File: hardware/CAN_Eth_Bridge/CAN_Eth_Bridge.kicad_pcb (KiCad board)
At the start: 2 copper layers, 60 x 100 mm, 161 parts, among them J101 Main Current Hall Sensor, J102 Global LV and CAN, J103 HRLV, J105 Conn_02x05_Odd_Even, J106 uart, J107 Micro_SD_Card, J301 RJ45_Amphenol_RJMG1BD3B8K1ANR, K101 G5Q-1A 24Vdc, Q101 MMBT5550L, Q102 MMBT5550L, Q103 MMBT5550L, Q301 MMBT5550L, Q302 MMBT5550L, Q501 MMBT5550L, Q502 MMBT5550L, U101 MCP2542FDxMF, U102 MCP2542FDxMF, U105 XM0G3507QPTRQ1, U201 Si1450DH, U202 LM74502, U203 Si1450DH, U204 AP64060ZQ, U205 AP64060ZQ, U301 W5500, U401 MCP1501-40xSN, U402 TLV713185PDBV, U404 MCP33151, U405 MCP33151, U408 Si1450DH, U409 NCV68061, U501 NSI5030, U502 Si1450DH, U503 NCV68061, U504 MCP2542FDxMF, U505 AP7384-50SA, U506 ISOM8110, U507 ISOM8110, U508 STISO620, Y301 Crystal_GND24

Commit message: long 88 can stick
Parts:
- removed C201, C208, C321, C401, C402, C403, C404, C408, C409, C410, C501, C504, C505, C506: 220n, Capacitor_SMD:C_0805_2012Metric_Pad1.18x1.45mm_HandSolder
- removed C203, C205, C206, C207, C209, C211, C212, C213: 10u, Capacitor_SMD:C_1206_3216Metric_Pad1.33x1.80mm_HandSolder
- removed C204, C210: 100n, Capacitor_SMD:C_1206_3216Metric_Pad1.33x1.80mm_HandSolder
- removed C406: 10n, Capacitor_SMD:C_0805_2012Metric_Pad1.18x1.45mm_HandSolder
- removed C502, C503: 1u, Capacitor_SMD:C_1206_3216Metric_Pad1.33x1.80mm_HandSolder
- removed D102, D201, D202: green, LED_SMD:LED_0805_2012Metric_Pad1.15x1.40mm_HandSolder
- removed D203, D204: ES1D, Diode_SMD:D_SMA
- removed D501, D502, D503: TS4148, Diode_SMD:D_0805_2012Metric_Pad1.15x1.40mm_HandSolder
- removed D504: 10V, Diode_SMD:D_0805_2012Metric_Pad1.15x1.40mm_HandSolder
- removed F101: ~1A, Fuse:Fuseholder_Blade_Mini_Keystone_3568
- removed J103: HRLV, Connector_Molex:Molex_Micro-Fit_3.0_43045-0600_2x03_P3.00mm_Horizontal
- removed J105: Conn_02x05_Odd_Even, Connector_PinHeader_1.27mm:PinHeader_2x05_P1.27mm_Vertical_SMD
- removed J106: uart, Connector_PinHeader_2.54mm:PinHeader_1x03_P2.54mm_Vertical
- removed J107: Micro_SD_Card, Connector_Card:microSD_HC_Wuerth_693072010801
- removed K101: G5Q-1A 24Vdc, Relay_THT:Relay_SPST_Omron-G5Q-1A
- removed L201, L202: 10u, Inductor_SMD:L_1210_3225Metric_Pad1.42x2.65mm_HandSolder
- removed Q101, Q102, Q103, Q501, Q502: MMBT5550L, Package_TO_SOT_SMD:SOT-23
- removed R1, R2, R505: 100, Resistor_SMD:R_1206_3216Metric_Pad1.30x1.75mm_HandSolder
- removed R102, R201: 4.99k, Resistor_SMD:R_1206_3216Metric_Pad1.30x1.75mm_HandSolder
- removed R104, R202, R501: 88.7k, Resistor_SMD:R_0805_2012Metric_Pad1.20x1.40mm_HandSolder
- removed R105, R203, R204: 3.32k, Resistor_SMD:R_0805_2012Metric_Pad1.20x1.40mm_HandSolder
- removed R106: 49.9, Resistor_SMD:R_0805_2012Metric_Pad1.20x1.40mm_HandSolder
- removed R205: 140k, Resistor_SMD:R_0805_2012Metric_Pad1.20x1.40mm_HandSolder
- removed R206, R208, R211: 22.1k, Resistor_SMD:R_0805_2012Metric_Pad1.20x1.40mm_HandSolder
- removed R207: 88.7kR, Resistor_SMD:R_0805_2012Metric_Pad1.20x1.40mm_HandSolder
- removed R209, R212: 4.7, Resistor_SMD:R_1206_3216Metric_Pad1.30x1.75mm_HandSolder
- removed R210: 51k, Resistor_SMD:R_0805_2012Metric_Pad1.20x1.40mm_HandSolder
- removed R404, R405: 14.3, Resistor_SMD:R_0805_2012Metric_Pad1.20x1.40mm_HandSolder
- removed R502, R503, R506: 2.4k, Resistor_SMD:R_0805_2012Metric_Pad1.20x1.40mm_HandSolder
- removed U105: XM0G3507QPTRQ1, zzLocalLibraries-Footprints:PT0048A-IPC_B
- removed U201, U203, U408: Si1450DH, Package_TO_SOT_SMD:SOT-363_SC-70-6_Handsoldering
- removed U202: LM74502, Package_TO_SOT_SMD:SOT-23-8_Handsoldering
- removed U204, U205: AP64060ZQ, Package_TO_SOT_SMD:TSOT-23-6
- removed U401: MCP1501-40xSN, Package_SO:SOIC-8_3.9x4.9mm_P1.27mm
- removed U402: TLV713185PDBV, Package_TO_SOT_SMD:SOT-23-5
- removed U404, U405: MCP33151, Package_SO:MSOP-10_3x3mm_P0.5mm
- removed U409, U503: NCV68061, Package_TO_SOT_SMD:TSOT-23-6
- removed U501: NSI5030, Diode_SMD:Nexperia_CFP3_SOD-123W
- removed U502: Si1450DH, Package_TO_SOT_SMD:SOT-363_SC-70-6
- removed U504: MCP2542FDxMF, Package_SO:SOIC-8_3.9x4.9mm_P1.27mm
- removed U505: AP7384-50SA, Package_TO_SOT_SMD:SOT-23
- removed U506, U507: ISOM8110, zzLocalLibraries-Footprints:ISOM811_SOIC-4_DFG
- removed U508: STISO620, Package_SO:SOIC-8_7.5x5.85mm_P1.27mm
- added C103: 220n, Capacitor_SMD:C_0805_2012Metric_Pad1.18x1.45mm_HandSolder, F.Cu at (94.9, 114.6)
- added FL102: Choke_CommonMode_FerriteCore_1243, Inductor_SMD:L_CommonModeChoke_Coilcraft_1812CAN, F.Cu at (112.1, 116.0)
- added SW102: SW_DIP_x06, Button_Switch_SMD:SW_DIP_SPSTx06_Slide_Copal_CHS-06B_W7.62mm_P1.27mm, F.Cu at (97.9, 107.9)
- added U103: XMSM0G3507SDGS28R, zzLocalLibraries-Footprints:VSSOP28_DGS_TEX-M, F.Cu at (107.5, 107.2)
- added U104: AP7381-33SA-7, Package_TO_SOT_SMD:SOT-23, F.Cu at (105.7, 114.3)
- J101: value Main Current Hall Sensor -> Conn_01x05_Pin; footprint Connector_Molex:Molex_Micro-Fit_3.0_43045-0400_2x02_P3.00mm_Horizontal -> Connector_PinHeader_2.54mm:PinHeader_1x05_P2.54mm_Vertical
- U102: value MCP2542FDxMF -> AP7384-50SA; footprint Package_SO:SOIC-8_3.9x4.9mm_P1.27mm -> Package_TO_SOT_SMD:SOT-23-3
- moved H103 108.6 mm to (100.9, 89.4)
- moved C101 100.3 mm to (94.5, 78.9), turned to 0 degrees
- moved C102 98.0 mm to (94.5, 82.0), turned to 0 degrees
- moved U102 91.5 mm to (99.5, 99.0), turned to 0 degrees
- moved C104 84.7 mm to (94.5, 85.0), turned to 0 degrees
- moved H102 81.8 mm to (100.9, 81.4)
- moved C110 80.8 mm to (94.5, 94.0)
- moved C109 80.6 mm to (94.5, 91.0)
- moved C108 79.9 mm to (94.5, 88.0), turned to 0 degrees
- moved U101 76.1 mm to (109.1, 96.0)
- moved J102 75.2 mm to (147.7, 137.9), turned to 180 degrees
- moved R111 73.5 mm to (99.9, 95.0), turned to 0 degrees
- moved R108 70.7 mm to (112.1, 81.9)
- moved D104 70.0 mm to (107.3, 85.0), turned to 0 degrees
- moved R110 68.7 mm to (112.1, 87.8), turned to 0 degrees
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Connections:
- C101 pad 1: +5V -> +3.3V
- C102 pad 1: +3.3V -> +5V
- D101 pad 1: LV+ -> Net-(D101-K)
- D101 pad 2: Net-(D101-A) -> /GLV+
- J101 pad 1: /MCHall_5Vin -> GND
- J101 pad 2: GND -> /prog.uart_ui_rx
- J101 pad 3: /MCHall_imprecise -> /prog.uart_ui_tx
- J101 pad 4: /MCHall_percise -> /prog.SWDIO
- J102 pad 4: /G_IL- -> /G_IL+
- U101 pad 6: /G_CAN- -> Net-(U101-CANL)
- U101 pad 7: /G_CAN+ -> Net-(U101-CANH)
- U102 pad 1: /HRLV interface/CAN_RX -> Net-(D101-K)
- U102 pad 2: GND -> +5V
- U102 pad 3: +5V -> GND
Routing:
- net (no net): track 0.00 -> 186.6 mm, vias 0 -> 2
- net +3.3V: track 304.3 -> 132.7 mm, vias 9 -> 2
- net +5V: track 124.4 -> 0.00 mm
- net LV+: track 80.2 -> 0.00 mm
- net /G_CAN+: track 67.4 -> 0.00 mm, vias 2 -> 0
- net /G_CAN-: track 67.4 -> 0.00 mm, vias 2 -> 0
- net /HRLV interface/+5V: track 66.0 -> 0.00 mm
- net /HRLV interface/LV+: track 54.7 -> 0.00 mm
- net /hrlv.pres_hrlv: track 48.2 -> 0.00 mm, vias 2 -> 0
- net /IL.forward: track 47.6 -> 0.00 mm
- net Net-(D102-K): track 41.4 -> 0.00 mm
- net /GLV PSU/GLV+: track 41.2 -> 0.00 mm
- net /hrlv.pres_interlock: track 37.3 -> 0.00 mm, vias 2 -> 0
- net /prog.uart_ui_rx: track 29.2 -> 4.57 mm, vias 2 -> 0
- net /Main Current Hall Sensing/4.096Vref: track 23.9 -> 0.00 mm
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- removed copper zone on F.Cu, net /GLV PSU/passing
- removed copper zone on B.Cu, net /G_IL+
- removed copper zone on F.Cu, net /G_IL+
- removed copper zone on B.Cu, net /G_IL-
- removed copper zone on F.Cu, net /G_IL-
- removed copper zone on B.Cu, net /HRLV_LV-
- removed copper zone on F.Cu, net /HRLV_LV-
- removed copper zone on F.Cu, net /vcore
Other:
- board size 60 x 100 mm -> 23 x 85 mm
- board text removed: "600Vdc galv ISO"
- board text removed: "CAN+"
- board text removed: "CAN-"
- board text removed: "GLV+ (9,34)V"
- board text removed: "GLV-"
- board text removed: "HRLV interface"
- board text removed: "IL return"
- board text removed: "IL_B"
- board text removed: "LV+ (5.5 , 35)V"
- board text removed: "LV-"
- board text removed: "bms fault"
- board text removed: "fuse ~800mA"
- board text removed: "ground loop from LV bulk to diode crosses sense line"
- board text removed: "indicator 2"

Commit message: shuffled
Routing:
- net (no net): track 186.6 -> 2.53 mm, vias 2 -> 0
- net /eth.MOSI/PICO: track 20.2 -> 1.71 mm, vias 2 -> 0
- net /eth.MISO/POCI: track 18.2 -> 2.49 mm, vias 2 -> 0
- net +3.3V: track 132.7 -> 117.0 mm, vias 2 -> 1
- net /eth.irq_N: track 15.5 -> 0.05 mm
- net /eth.reset_N: track 14.5 -> 0.00 mm
- net /eth.SCLK: track 17.5 -> 3.05 mm
- net /eth.cs_N: track 18.5 -> 5.93 mm
- net GND: track 24.7 -> 16.7 mm, vias 82 -> 61
- net /G_IL+: track 5.27 -> 0.00 mm
- net /prog.uart_ui_tx: track 4.67 -> 0.00 mm
- net /prog.uart_ui_rx: track 4.57 -> 0.00 mm
- net /GLV+: track 2.73 -> 0.00 mm
- removed copper zone on F.Cu, net +3.3V
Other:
- board size 23 x 85 mm -> 22.6 x 85 mm
- board text removed: "indicator 1"
- board text removed: "scheduler"

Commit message: hdd failure D:
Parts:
- removed C102, C108, C109, C110, C315: 220n, Capacitor_SMD:C_0805_2012Metric_Pad1.18x1.45mm_HandSolder
- removed C107: 10u, Capacitor_SMD:C_1206_3216Metric_Pad1.33x1.80mm_HandSolder
- removed C307, C308, C310: 100n, Capacitor_SMD:C_0603_1608Metric_Pad1.08x0.95mm_HandSolder
- removed D103, D104: yellow, LED_SMD:LED_0805_2012Metric_Pad1.15x1.40mm_HandSolder
- removed D106: blue, LED_SMD:LED_0805_2012Metric_Pad1.15x1.40mm_HandSolder
- removed FL102: Choke_CommonMode_FerriteCore_1243, Inductor_SMD:L_CommonModeChoke_Coilcraft_1812CAN
- removed H101, H102, H103: MountingHole, MountingHole:MountingHole_3.2mm_M3
- removed R107, R108, R109: 2.4k, Resistor_SMD:R_0805_2012Metric_Pad1.20x1.40mm_HandSolder
- removed R110: 3.32k, Resistor_SMD:R_0805_2012Metric_Pad1.20x1.40mm_HandSolder
- removed R111: 100k, Resistor_SMD:R_1206_3216Metric_Pad1.30x1.75mm_HandSolder
- removed R112: 40.2k, Resistor_SMD:R_0805_2012Metric_Pad1.20x1.40mm_HandSolder
- removed R304, R305, R307, R308: 14.3, Resistor_SMD:R_0805_2012Metric_Pad1.20x1.40mm_HandSolder
- removed R306: 10, Resistor_SMD:R_0805_2012Metric_Pad1.20x1.40mm_HandSolder
- removed SW102: SW_DIP_x06, Button_Switch_SMD:SW_DIP_SPSTx06_Slide_Copal_CHS-06B_W7.62mm_P1.27mm
- added C105: 10u, Capacitor_SMD:C_1206_3216Metric_Pad1.33x1.80mm_HandSolder, F.Cu at (152.3, 111.7)
- added C106: 220n, Capacitor_SMD:C_0805_2012Metric_Pad1.18x1.45mm_HandSolder, B.Cu at (152.0, 107.4)
- added D102: green, LED_SMD:LED_0805_2012Metric_Pad1.15x1.40mm_HandSolder, F.Cu at (135.7, 120.0)
- added FL101: Choke_CommonMode_FerriteCore_1243, Inductor_SMD:L_CommonModeChoke_Coilcraft_1812CAN, B.Cu at (149.5, 118.4)
- added R102: 2.4k, Resistor_SMD:R_0805_2012Metric_Pad1.20x1.40mm_HandSolder, F.Cu at (135.7, 118.0)
- added R103: 2.4k, Resistor_SMD:R_0805_2012Metric_Pad1.20x1.40mm_HandSolder, F.Cu at (153.7, 118.4)
- added R104: 2.4k, Resistor_SMD:R_0805_2012Metric_Pad1.20x1.40mm_HandSolder, B.Cu at (153.0, 102.7)
- added R105: 100k, Resistor_SMD:R_1206_3216Metric_Pad1.30x1.75mm_HandSolder, B.Cu at (152.4, 104.8)
- C101, C103, C301, C311, D101, Q301, Q302, R315, R316, R317: moved to B.Cu
- D105: value red -> blue
- J101: value Conn_01x05_Pin -> Global LV and CAN; footprint Connector_PinHeader_2.54mm:PinHeader_1x05_P2.54mm_Vertical -> Connector_Molex:Molex_Micro-Fit_3.0_43045-0600_2x03_P3.00mm_Horizontal
- J102: value Global LV and CAN -> Conn_01x05_Pin; footprint Connector_Molex:Molex_Micro-Fit_3.0_43045-0600_2x03_P3.00mm_Horizontal -> Connector_PinHeader_2.54mm:PinHeader_1x05_P2.54mm_Vertical; moved to B.Cu
- R311, R312: value 4.99k -> 3.32k; footprint Resistor_SMD:R_1206_3216Metric_Pad1.30x1.75mm_HandSolder -> Resistor_SMD:R_0805_2012Metric_Pad1.20x1.40mm_HandSolder
- U101: value MCP2542FDxMF -> AP7384-50SA; footprint Package_SO:SOIC-8_3.9x4.9mm_P1.27mm -> Package_TO_SOT_SMD:SOT-23-3
- U102: value AP7384-50SA -> AP7381-33SA-7; footprint Package_TO_SOT_SMD:SOT-23-3 -> Package_TO_SOT_SMD:SOT-23
- U103: value XMSM0G3507SDGS28R -> MCP2542FDxMF; footprint zzLocalLibraries-Footprints:VSSOP28_DGS_TEX-M -> Package_SO:SOIC-8_3.9x4.9mm_P1.27mm; moved to B.Cu
- U104: value AP7381-33SA-7 -> XMSM0G3507SDGS28R; footprint Package_TO_SOT_SMD:SOT-23 -> zzLocalLibraries-Footprints:VSSOP28_DGS_TEX-M
- moved C101 61.4 mm to (139.9, 120.3)
- moved C103 59.0 mm to (153.8, 119.5), turned to -90 degrees
- moved D105 56.5 mm to (153.7, 120.4), turned to 180 degrees
- moved C104 49.4 mm to (136.0, 111.8)
- moved D101 49.1 mm to (138.9, 116.6), turned to 90 degrees
- moved J102 49.1 mm to (154.2, 89.2)
- moved U101 48.5 mm to (153.7, 115.1), turned to -90 degrees
- moved U104 46.9 mm to (151.8, 105.7), turned to 180 degrees
- moved U103 45.1 mm to (152.2, 112.7), turned to -90 degrees
- moved U102 39.5 mm to (135.7, 115.0), turned to -90 degrees
- moved J101 34.6 mm to (147.7, 114.5), turned to 180 degrees
- moved Q301 17.3 mm to (143.1, 68.7), turned to 0 degrees
- moved R316 16.4 mm to (144.8, 65.5), turned to 180 degrees
- moved R317 15.1 mm to (146.9, 71.4)
- moved Q302 10.0 mm to (143.1, 72.4), turned to 0 degrees
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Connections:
- C101 pad 1: +3.3V -> Net-(D101-K)
- C103 pad 1: Net-(D101-K) -> +5V
- C104 pad 1: +5V -> +3.3V
- C316 pad 1: /Ethernet/RX_1+ -> /Ethernet/RX+
- C317 pad 1: /Ethernet/RX_1- -> /Ethernet/RX-
- D105 pad 1: GND -> Net-(D105-K)
- D105 pad 2: Net-(D105-A) -> /led.sched
- J101 pad 1: GND -> /G_IL+
- J101 pad 2: /prog.uart_ui_rx -> GND
- J101 pad 3: /prog.uart_ui_tx -> /G_CAN-
- J101 pad 4: /prog.SWDIO -> /G_IL+
- J101 pad 5: /prog.SWCLK -> /GLV+
- J102 pad 1: /G_IL+ -> GND
- J102 pad 2: GND -> /prog.uart_ui_tx
- J102 pad 3: /G_CAN- -> /prog.uart_ui_rx
- J102 pad 4: /G_IL+ -> /prog.SWDIO
- J102 pad 5: /GLV+ -> /prog.SWCLK
- R310 pad 2: /Ethernet/RX_1- -> /Ethernet/RX-
- R314 pad 2: /Ethernet/RX_1+ -> /Ethernet/RX+
- U101 pad 1: /can.tx -> Net-(D101-K)
- U101 pad 2: GND -> +5V
- U101 pad 3: +5V -> GND
- U102 pad 2: +5V -> +3.3V
- U103 pad 1: unconnected-(U103-PA26/A0_1-Pad1) -> /can.tx
- U103 pad 2: unconnected-(U103-PA27/RTC_OUT/A0_0-Pad2) -> GND
- U103 pad 3: /vcore -> +5V
- U103 pad 4: unconnected-(U103-PA0-Pad4) -> /can.rx
- U103 pad 5: unconnected-(U103-PA1-Pad5) -> +3.3V
- U103 pad 7: +3.3V -> Net-(U103-CANH)
- U104 pad 1: Net-(D101-K) -> /can.tx
- U104 pad 2: +3.3V -> /can.rx
- U104 pad 3: GND -> /vcore
- U301 pad 1: /Ethernet/TX- -> /Ethernet/TD-
- U301 pad 2: /Ethernet/TX+ -> /Ethernet/TD+
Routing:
- net /Ethernet/+3.3VA: track 102.0 -> 66.8 mm, vias 4 -> 6
- net Net-(D101-K): track 0.00 -> 32.6 mm, vias 0 -> 1
- net /led.i1: track 0.00 -> 24.5 mm, vias 0 -> 2
- net GND: track 16.7 -> 37.5 mm, vias 61 -> 48
- net Net-(Q301-B): track 26.9 -> 44.9 mm, vias 0 -> 1
- net /led.sched: track 0.00 -> 16.0 mm
- net /prog.uart_ui_tx: track 0.00 -> 13.8 mm, vias 0 -> 1
- net Net-(J301-PadL3): track 16.5 -> 3.12 mm
- net Net-(J301-PadL2): track 15.7 -> 2.42 mm
- net /prog.uart_ui_rx: track 0.00 -> 12.5 mm, vias 0 -> 1
- net /prog.SWDIO: track 0.00 -> 12.4 mm, vias 0 -> 1
- net /prog.SWCLK: track 0.00 -> 11.2 mm, vias 0 -> 1
- net /GLV+: track 0.00 -> 10.4 mm, vias 0 -> 1
- net /G_CAN+: track 0.00 -> 9.73 mm, vias 0 -> 1
- net +5V: track 0.00 -> 9.16 mm, vias 0 -> 2
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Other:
- board size 22.6 x 85 mm -> 22.6 x 60.7 mm
- board text added: "CAN-Ethernet bridge github.com/Gregification/BeeMS/ 2/8/2026 - pinning & design:"
- board text added: "SWCLK"
- board text added: "SWDIO"
- board text added: "hope and dreams kind of routing"
- board text removed: "5V out"
- board text removed: "E27 accumulator LV-ish garage top view"
- board text removed: "ETH"
- board text removed: "GLV"
- board text removed: "HRLV"
- board text removed: "HV cross path. AIRs(TSBPIRs?), main fuse,"
- board text removed: "LV connectors somewhere over here"
- board text removed: "MCHS"
- board text removed: "Master Board A 1.1 (testing use only) github.com/Gregification/BeeMS/ 1/13/2025 - pinning & hardware info: {dblquote}/hardware/MasterBoard_A/meta.xlsx{dblquote} - software: {dblquote}/MB_MSPM0G3507_A{dblquote} - no hardware watchdog - no PWM bank"
- board text removed: "Master Board go about here"
- board text removed: "PWM SB1"
- board text removed: "cut out to segments below"
- board text removed: "hope and dreams kind of wiring"
- board text removed: "impercise"
- board text removed: "not to scale"
- board text removed: "percise"
- board text removed: "we dont talk about this routing"

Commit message: civilized note taking
and untaking !?!?!
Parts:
- added G***: LOGO, LOGO, B.Cu at (140.9, 89.4)
- added G***: LOGO, zzLocalLibraries-Footprints:qrcode_wawa, B.Cu at (138.5, 106.0)
- added R101: 10, Resistor_SMD:R_0805_2012Metric_Pad1.20x1.40mm_HandSolder, B.Cu at (138.9, 114.5)
- moved C101 2.27 mm to (141.0, 118.3), turned to 90 degrees
- moved D101 1.70 mm to (138.9, 118.3)
- moved C311 1.30 mm to (148.6, 94.1), turned to -90 degrees
- turned R102 to 0 degrees
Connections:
- D101 pad 2: /GLV+ -> Net-(D101-A)
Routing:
- net /GLV+: track 10.4 -> 8.40 mm
- net Net-(D101-A): track 0.00 -> 1.77 mm
- net /led.i1: track 24.5 -> 25.9 mm
- net Net-(D101-K): track 32.6 -> 31.7 mm
- net Net-(D102-K): track 2.85 -> 2.04 mm
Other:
- board text added: "100MBs"
- board text added: "2/8/2026"
- board text added: "CAN-Eth bridge github.com/Gregification/BeeMS/"
- board text added: "INFO"
- board text added: "Other"
- board text added: "UT-Arlington Racing 2026"
- board text removed: "100MB/S ethernet"
- board text removed: "CAN-Ethernet bridge github.com/Gregification/BeeMS/ 2/8/2026 - pinning & design:"
- board text removed: "GLV interface"
- board text removed: "IL out"
- board text removed: "IL_A"
- board text removed: "trust me bro, length tuning can to mm match is essential"

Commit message: kil!
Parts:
- R302: value 14.3 -> 10
- R311, R312: value 3.32k -> 2.4k
- turned R311 to 0 degrees
- turned R312 to 0 degrees
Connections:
- R311 pad 1: Net-(U301-LINKLED) -> Net-(Q301-B)
- R311 pad 2: Net-(Q301-B) -> Net-(U301-LINKLED)
- R312 pad 1: Net-(U301-ACTLED) -> Net-(Q302-B)
- R312 pad 2: Net-(Q302-B) -> Net-(U301-ACTLED)
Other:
- board text added: "Can-bus Ethrenet Bridge"

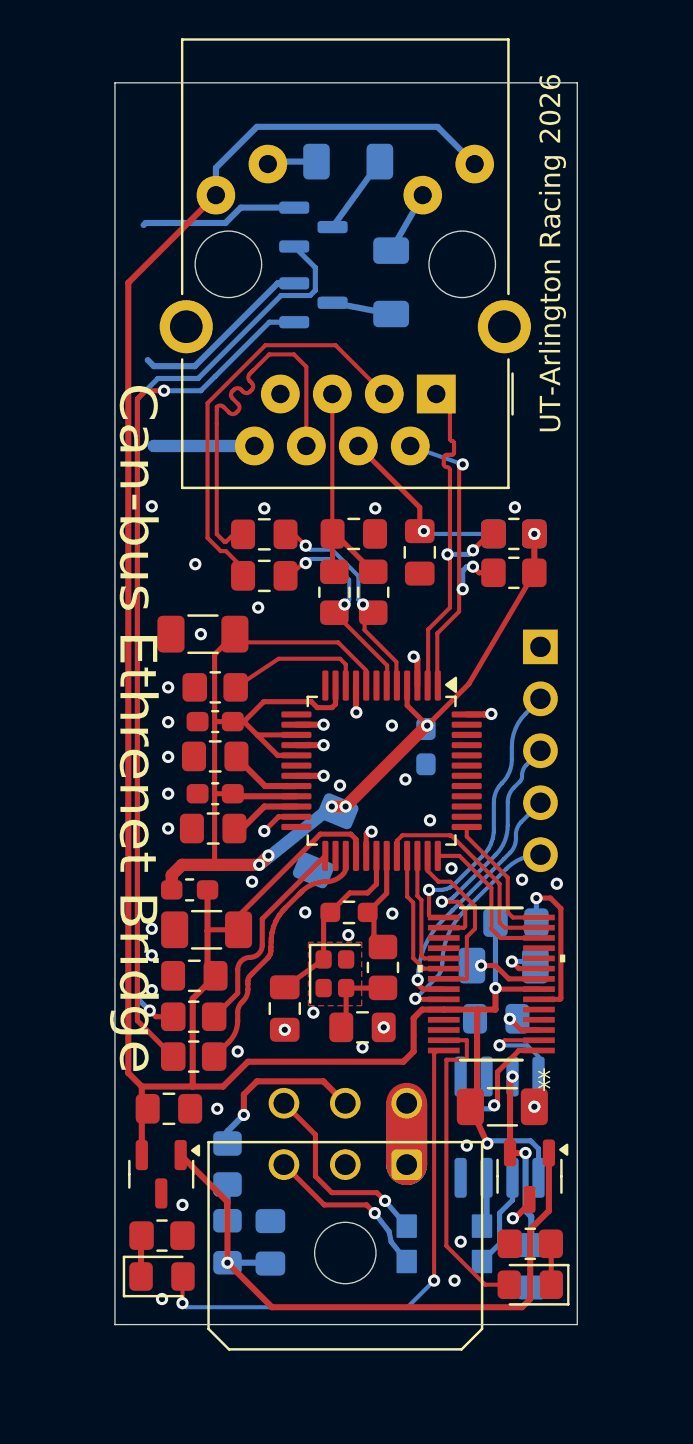
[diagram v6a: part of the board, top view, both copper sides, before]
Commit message: super 3v3 rail
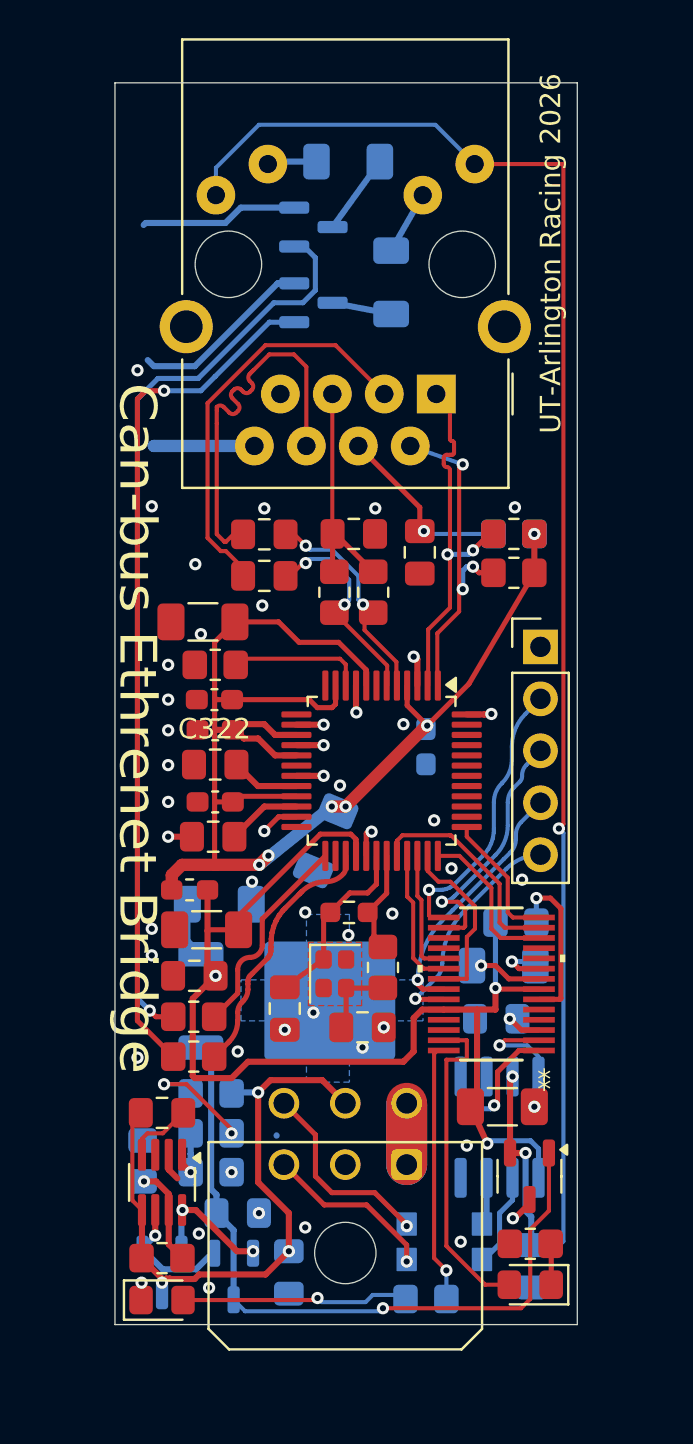
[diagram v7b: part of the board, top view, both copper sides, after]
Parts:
- removed C104: 220n, Capacitor_SMD:C_0805_2012Metric_Pad1.18x1.45mm_HandSolder
- removed D101: TS4148, Diode_SMD:D_0805_2012Metric_Pad1.15x1.40mm_HandSolder
- removed the G*** at (138.5, 106.0)
- removed R101: 10, Resistor_SMD:R_0805_2012Metric_Pad1.20x1.40mm_HandSolder
- removed U102: AP7381-33SA-7, Package_TO_SOT_SMD:SOT-23
- added C102: 220n, Capacitor_SMD:C_0805_2012Metric_Pad1.18x1.45mm_HandSolder, F.Cu at (135.7, 112.0)
- added C109: 220n, Capacitor_SMD:C_0805_2012Metric_Pad1.18x1.45mm_HandSolder, B.Cu at (141.9, 119.8)
- added C110: 220n, Capacitor_SMD:C_0805_2012Metric_Pad1.18x1.45mm_HandSolder, B.Cu at (139.4, 116.9)
- added C322: 100n, Capacitor_SMD:C_0603_1608Metric_Pad1.08x0.95mm_HandSolder, F.Cu at (138.3, 91.8)
- added Q101: TSM2328CX, Package_TO_SOT_SMD:SOT-23-3, B.Cu at (135.7, 119.8)
- added Q102: TSM2328CX, Package_TO_SOT_SMD:SOT-23-3, B.Cu at (139.2, 120.0)
- added R106: 88.7kR, Resistor_SMD:R_0805_2012Metric_Pad1.20x1.40mm_HandSolder, F.Cu at (135.7, 119.1)
- added R107: 3.32k, Resistor_SMD:R_0805_2012Metric_Pad1.20x1.40mm_HandSolder, B.Cu at (134.8, 114.3)
- added R108: 88.7kR, Resistor_SMD:R_0805_2012Metric_Pad1.20x1.40mm_HandSolder, B.Cu at (138.1, 113.0)
- added R109: 12.4k, Resistor_SMD:R_0805_2012Metric_Pad1.20x1.40mm_HandSolder, B.Cu at (138.1, 114.9)
- added R110: 12.4k, Resistor_SMD:R_0805_2012Metric_Pad1.20x1.40mm_HandSolder, B.Cu at (138.1, 111.0)
- added U105: LM74502, Package_TO_SOT_SMD:SOT-23-8_Handsoldering, F.Cu at (135.7, 115.4)
- added U106: BD33FC0FP, Package_TO_SOT_SMD:TO-252-2, B.Cu at (142.6, 106.5)
- C101: value 220n -> 10u; footprint Capacitor_SMD:C_0805_2012Metric_Pad1.18x1.45mm_HandSolder -> Capacitor_SMD:C_1206_3216Metric_Pad1.33x1.80mm_HandSolder
- J102: moved to F.Cu
- R102: moved to B.Cu
- R316, R317: value 332 -> 750
- moved C101 16.7 mm to (138.5, 101.8), turned to 0 degrees
- moved R102 13.3 mm to (148.6, 121.1)
- moved D102 1.15 mm to (135.7, 121.2)
- moved R303 1.10 mm to (138.3, 90.1)
- moved C302 0.60 mm to (137.7, 88.0)
- moved C305 0.40 mm to (138.3, 93.3)
- moved C312 0.40 mm to (138.2, 98.5)
- moved C304 0.40 mm to (138.3, 96.8)
- moved C314 0.40 mm to (138.3, 95.0)
- moved FL101 0.10 mm to (149.5, 118.3)
- turned J102 to 0 degrees
- turned R317 to 90 degrees
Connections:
- C101 pad 1: Net-(D101-K) -> +3.3V
- D102 pad 1: Net-(D102-K) -> GND
- D102 pad 2: /led.i1 -> Net-(D102-A)
- J301 pad L1: +3.3V -> +5V
- J301 pad L4: +3.3V -> +5V
- R102 pad 1: Net-(D102-K) -> Net-(D102-A)
- R102 pad 2: GND -> /led.i1
- R317 pad 1: Net-(J301-PadL3) -> Net-(Q302-C)
- R317 pad 2: Net-(Q302-C) -> Net-(J301-PadL3)
- U101 pad 1: Net-(D101-K) -> /LV+
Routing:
- net +5V: track 9.16 -> 83.6 mm, vias 2 -> 3
- net +3.3V: track 122.0 -> 59.1 mm, vias 2 -> 3
- net /LV+: track 0.00 -> 35.5 mm, vias 0 -> 1
- net Net-(D101-K): track 31.7 -> 0.00 mm, vias 1 -> 0
- net /GLV+: track 8.40 -> 31.3 mm, vias 1 -> 3
- net /led.i1: track 25.9 -> 12.9 mm, vias 2 -> 1
- net Net-(D102-A): track 0.00 -> 11.4 mm, vias 0 -> 1
- net Net-(Q101-G): track 0.00 -> 6.44 mm, vias 0 -> 1
- net /passing: track 0.00 -> 6.22 mm, vias 0 -> 2
- net Net-(R108-Pad2): track 0.00 -> 5.89 mm, vias 0 -> 2
- net Net-(U105-OV): track 0.00 -> 4.88 mm, vias 0 -> 1
- net /Ethernet/+3.3VA: track 66.8 -> 70.4 mm
- net Net-(U105-VCAP): track 0.00 -> 3.32 mm
- net Net-(U105-EN/UVLO): track 0.00 -> 2.92 mm, vias 0 -> 1
- net GND: track 37.5 -> 40.3 mm, vias 48 -> 50
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
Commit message: bridge v2
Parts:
- removed C109: 220n, Capacitor_SMD:C_0805_2012Metric_Pad1.18x1.45mm_HandSolder
- moved C110 3.75 mm to (141.9, 119.7), turned to 90 degrees
- moved C301 0.80 mm to (144.5, 98.7), turned to -90 degrees
- moved R107 0.65 mm to (134.8, 115.0)
- moved Q102 0.20 mm to (139.2, 119.8)
- moved G*** 0.10 mm to (140.9, 89.5)
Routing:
- net /LV+: track 35.5 -> 36.1 mm
- net /GLV+: track 31.3 -> 30.8 mm, vias 3 -> 2
- net +5V: track 83.6 -> 83.5 mm, vias 3 -> 2
- net GND: vias 50 -> 51
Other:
- board text added: "±65Vmax, (11,34)V working"
- board text removed: "100MBs"
- board text removed: "Can-bus Ethrenet Bridge"
- board text removed: "INFO"
- board text removed: "Other"
